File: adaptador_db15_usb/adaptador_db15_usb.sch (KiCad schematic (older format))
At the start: 3 parts, among them J1 Conn_01x34, J2 A-USB3_A-LP-SMT1, J3 A-USB3_A-LP-SMT1

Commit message: Fixed adapter pins connections
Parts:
- J2, J3: symbol A-USB3_A-LP-SMT1:A-USB3_A-LP-SMT1 -> adaptador_db15_usb-rescue:A-USB3_A-LP-SMT1-A-USB3_A-LP-SMT1
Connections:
- wire segments 70 -> 122
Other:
- moved on the sheet: J1
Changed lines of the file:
@@
 EESchema Schematic File Version 4
-LIBS:adaptador_db15_usb-cache
-EELAYER 26 0
+EELAYER 30 0
 EELAYER END
 $Descr A4 11693 8268
@@
 L Connector_Generic:Conn_01x34 J1
 U 1 1 60786015
-P 3550 4300
-F 0 "J1" H 3470 6117 50  0000 C CNN
-F 1 "Conn_01x34" H 3470 6026 50  0000 C CNN
-F 2 "kl25z:DSUB-15-HD_F_D" H 3550 4300 50  0001 C CNN
-F 3 "~" H 3550 4300 50  0001 C CNN
-	1    3550 4300
+P 2589 4300
+F 0 "J1" H 2509 6117 50  0000 C CNN
+F 1 "Conn_01x34" H 2509 6026 50  0000 C CNN
+F 2 "kl25z:DSUB-15-HD_F_D" H 2589 4300 50  0001 C CNN
+F 3 "~" H 2589 4300 50  0001 C CNN
+	1    2589 4300
 	-1   0    0    -1
 $EndComp
 $Comp
-L A-USB3_A-LP-SMT1:A-USB3_A-LP-SMT1 J2
+L adaptador_db15_usb-rescue:A-USB3_A-LP-SMT1-A-USB3_A-LP-SMT1 J2
 U 1 1 607860AA
 P 7000 3250
@@
 $EndComp
 $Comp
-L A-USB3_A-LP-SMT1:A-USB3_A-LP-SMT1 J3
+L adaptador_db15_usb-rescue:A-USB3_A-LP-SMT1-A-USB3_A-LP-SMT1 J3
 U 1 1 60786146
 P 7000 4750
@@
 $EndComp
 Wire Wire Line
-	3750 5700 4100 5700
-Wire Wire Line
 	4100 5700 4100 5800
-Wire Wire Line
-	4100 6000 3750 6000
-Wire Wire Line
-	3750 5800 4100 5800
 Connection ~ 4100 5800
 Wire Wire Line
 	4100 5800 4100 5900
-Wire Wire Line
-	3750 5900 4100 5900
 Connection ~ 4100 5900
 Wire Wire Line
@@
 EndData
 $EndBitmap
-Wire Wire Line
-	3750 3800 4500 3800
 Text Label 4050 3000 0    50   ~ 0
 up1
@@
 Text Label 4050 4100 0    50   ~ 0
 -clock1
-Wire Wire Line
-	3750 4200 4500 4200
-Wire Wire Line
-	3750 4400 4500 4400
-Wire Wire Line
-	4500 4700 3750 4700
-Wire Wire Line
-	3750 4800 4500 4800
-Wire Wire Line
-	4500 5000 3750 5000
-Wire Wire Line
-	4500 5200 3750 5200
-Wire Wire Line
-	3750 5300 4500 5300
-Wire Wire Line
-	3750 5500 4500 5500
 Text Label 3750 4200 0    50   ~ 0
 [1]
@@
 NoConn ~ 6600 2750
 Wire Wire Line
-	3750 3100 5500 3100
-Wire Wire Line
 	5500 3100 5500 3450
 Wire Wire Line
 	5500 3450 6600 3450
 Wire Wire Line
-	3750 3900 5550 3900
-Wire Wire Line
 	5550 3900 5550 3550
 Wire Wire Line
 	5550 3550 6600 3550
 Wire Wire Line
-	3750 3400 5550 3400
-Wire Wire Line
 	5550 3400 5550 3150
 Wire Wire Line
 	5550 3150 6600 3150
 Wire Wire Line
-	3750 4100 5600 4100
-Wire Wire Line
 	5600 4100 5600 3250
 Wire Wire Line
@@
 	5450 2850 6600 2850
 Wire Wire Line
-	3750 3600 5450 3600
-Wire Wire Line
 	5400 2800 5400 2950
 Wire Wire Line
 	5400 2950 6250 2950
-Wire Wire Line
-	3750 2800 5400 2800
 Wire Wire Line
 	6600 3050 6250 3050
@@
 Wire Wire Line
 	5350 3350 6600 3350
-Wire Wire Line
-	3750 3000 5350 3000
 NoConn ~ 4500 3800
 Wire Wire Line
@@
 	5350 4850 6600 4850
 Wire Wire Line
-	3750 4300 5400 4300
-Wire Wire Line
-	3750 4500 5350 4500
-Wire Wire Line
-	3750 4600 5500 4600
-Wire Wire Line
-	3750 4900 5550 4900
-Wire Wire Line
-	3750 5100 5450 5100
-Wire Wire Line
-	3750 5400 5550 5400
-Wire Wire Line
-	3750 5600 5600 5600
-Wire Wire Line
 	6600 5250 6600 5700
 Connection ~ 6600 5700
 Wire Wire Line
 	6600 5700 8650 5700
+Wire Wire Line
+	2789 5700 4100 5700
+Wire Wire Line
+	2789 6000 4100 6000
+Wire Wire Line
+	2789 5800 4100 5800
+Wire Wire Line
+	2789 5900 4100 5900
+Wire Wire Line
+	3140 2700 3140 4200
+Wire Wire Line
+	3159 2800 3159 4300
+Wire Wire Line
+	3179 2900 3179 4400
+Wire Wire Line
+	3199 3000 3199 4500
+Wire Wire Line
+	3219 3100 3219 4600
+Wire Wire Line
+	3239 3200 3239 4700
+Wire Wire Line
+	3258 3300 3258 4800
+Wire Wire Line
+	3278 3400 3278 4900
+Wire Wire Line
+	3298 3500 3298 5000
+Wire Wire Line
+	3318 3600 3318 5100
+Wire Wire Line
+	3339 3700 3339 5200
+Wire Wire Line
+	3358 3800 3358 5300
+Wire Wire Line
+	3378 3900 3378 5400
+Wire Wire Line
+	3398 4000 3398 5500
+Wire Wire Line
+	3418 4100 3418 5600
+Wire Wire Line
+	2789 2700 3140 2700
+Wire Wire Line
+	2789 2800 3159 2800
+Wire Wire Line
+	2789 2900 3179 2900
+Wire Wire Line
+	2789 3000 3199 3000
+Wire Wire Line
+	2789 3100 3219 3100
+Wire Wire Line
+	2789 3200 3239 3200
+Wire Wire Line
+	2789 3300 3258 3300
+Wire Wire Line
+	2789 3400 3278 3400
+Wire Wire Line
+	2789 3500 3298 3500
+Wire Wire Line
+	2789 3600 3318 3600
+Wire Wire Line
+	2789 3700 3339 3700
+Wire Wire Line
+	2789 3800 3358 3800
+Wire Wire Line
+	2789 3900 3378 3900
+Wire Wire Line
+	2789 4000 3398 4000
+Wire Wire Line
+	2789 4100 3418 4100
+Wire Wire Line
+	2789 4200 3140 4200
+Wire Wire Line
+	2789 4400 3179 4400
+Wire Wire Line
+	2789 4700 3239 4700
+Wire Wire Line
+	2789 4800 3258 4800
+Wire Wire Line
+	2789 5000 3298 5000
+Wire Wire Line
+	2789 5200 3339 5200
+Wire Wire Line
+	2789 5300 3358 5300
+Wire Wire Line
+	2789 5500 3398 5500
+Wire Wire Line
+	2789 4300 3159 4300
+Wire Wire Line
+	2789 4500 3199 4500
+Wire Wire Line
+	2789 4600 3219 4600
+Wire Wire Line
+	2789 4900 3278 4900
+Wire Wire Line
+	2789 5100 3318 5100
+Wire Wire Line
+	2789 5400 3378 5400
+Wire Wire Line
+	2789 5600 3418 5600
+Connection ~ 3140 2700
+Wire Wire Line
+	3140 2700 3750 2700
+Connection ~ 3140 4200
+Wire Wire Line
+	3140 4200 4500 4200
+Connection ~ 3159 2800
+Wire Wire Line
+	3159 2800 5400 2800
+Connection ~ 3159 4300
+Wire Wire Line
+	3159 4300 5400 4300
+Connection ~ 3179 2900
+Wire Wire Line
+	3179 2900 3750 2900
+Connection ~ 3179 4400
+Wire Wire Line
+	3179 4400 4500 4400
+Connection ~ 3199 3000
+Wire Wire Line
+	3199 3000 5350 3000
+Connection ~ 3199 4500
+Wire Wire Line
+	3199 4500 5350 4500
+Connection ~ 3219 3100
+Wire Wire Line
+	3219 3100 5500 3100
+Connection ~ 3219 4600
+Wire Wire Line
+	3219 4600 5500 4600
+Connection ~ 3239 3200
+Wire Wire Line
+	3239 3200 3750 3200
+Connection ~ 3239 4700
+Wire Wire Line
+	3239 4700 4500 4700
+Connection ~ 3258 3300
+Wire Wire Line
+	3258 3300 3750 3300
+Connection ~ 3258 4800
+Wire Wire Line
+	3258 4800 4500 4800
+Connection ~ 3278 3400
+Wire Wire Line
+	3278 3400 5550 3400
+Connection ~ 3278 4900
+Wire Wire Line
+	3278 4900 5550 4900
+Connection ~ 3298 3500
+Wire Wire Line
+	3298 3500 3750 3500
+Connection ~ 3298 5000
+Wire Wire Line
+	3298 5000 4500 5000
+Connection ~ 3318 3600
+Wire Wire Line
+	3318 3600 5450 3600
+Connection ~ 3318 5100
+Wire Wire Line
+	3318 5100 5450 5100
+Connection ~ 3339 3700
+Wire Wire Line
+	3339 3700 3750 3700
+Connection ~ 3339 5200
+Wire Wire Line
+	3339 5200 4500 5200
+Connection ~ 3358 3800
+Wire Wire Line
+	3358 3800 4500 3800
+Connection ~ 3358 5300
+Wire Wire Line
+	3358 5300 4500 5300
+Connection ~ 3378 3900
+Wire Wire Line
+	3378 3900 5550 3900
+Connection ~ 3378 5400
+Wire Wire Line
+	3378 5400 5550 5400
+Connection ~ 3398 4000
+Wire Wire Line
+	3398 4000 3750 4000
+Connection ~ 3398 5500
+Wire Wire Line
+	3398 5500 4500 5500
+Connection ~ 3418 4100
+Wire Wire Line
+	3418 4100 5600 4100
+Connection ~ 3418 5600
+Wire Wire Line
+	3418 5600 5600 5600
 $EndSCHEMATC

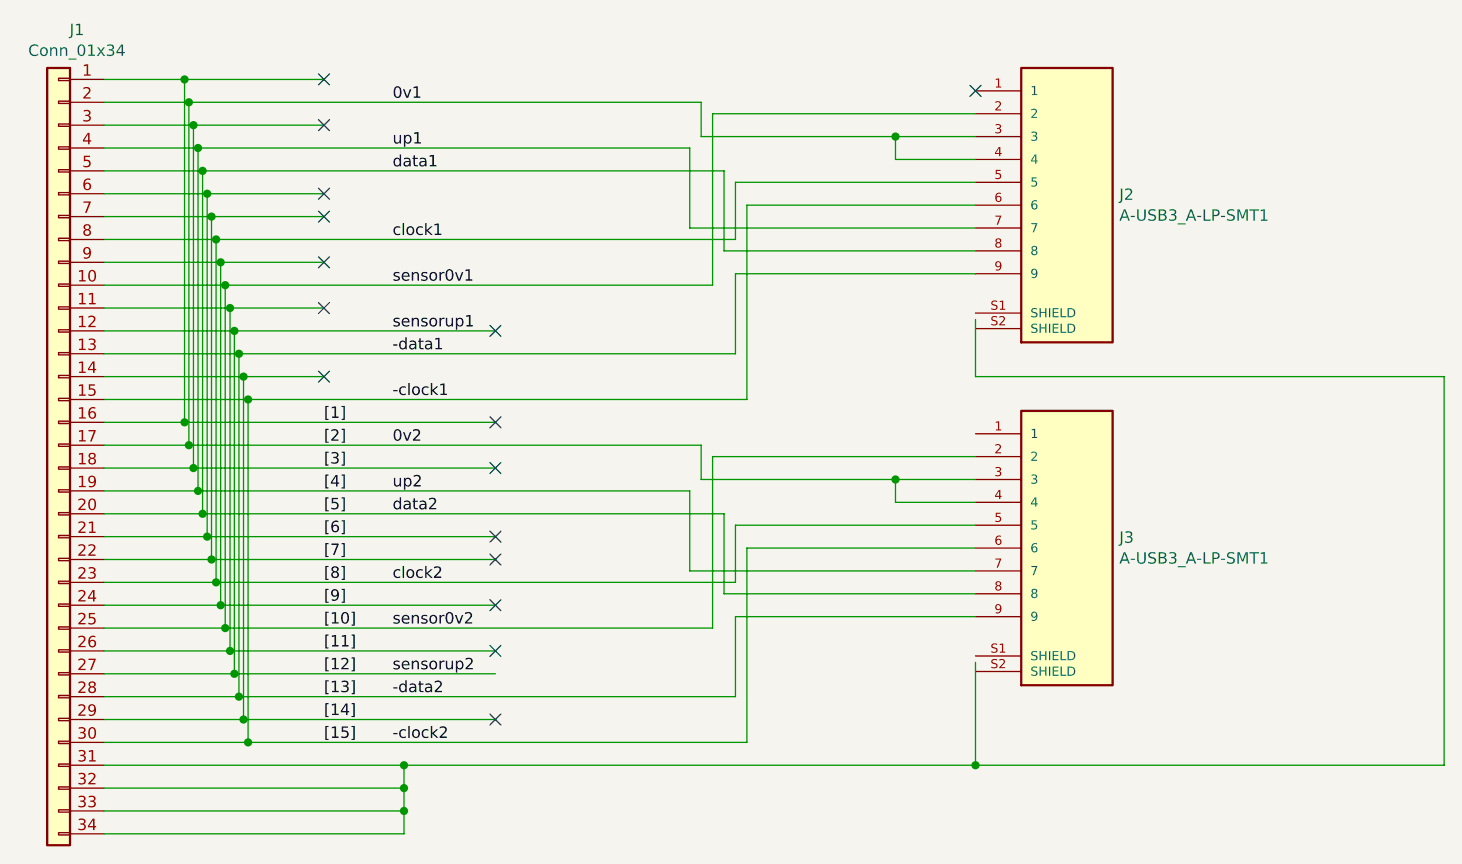
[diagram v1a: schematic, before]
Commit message: Fixed adapter pins connections
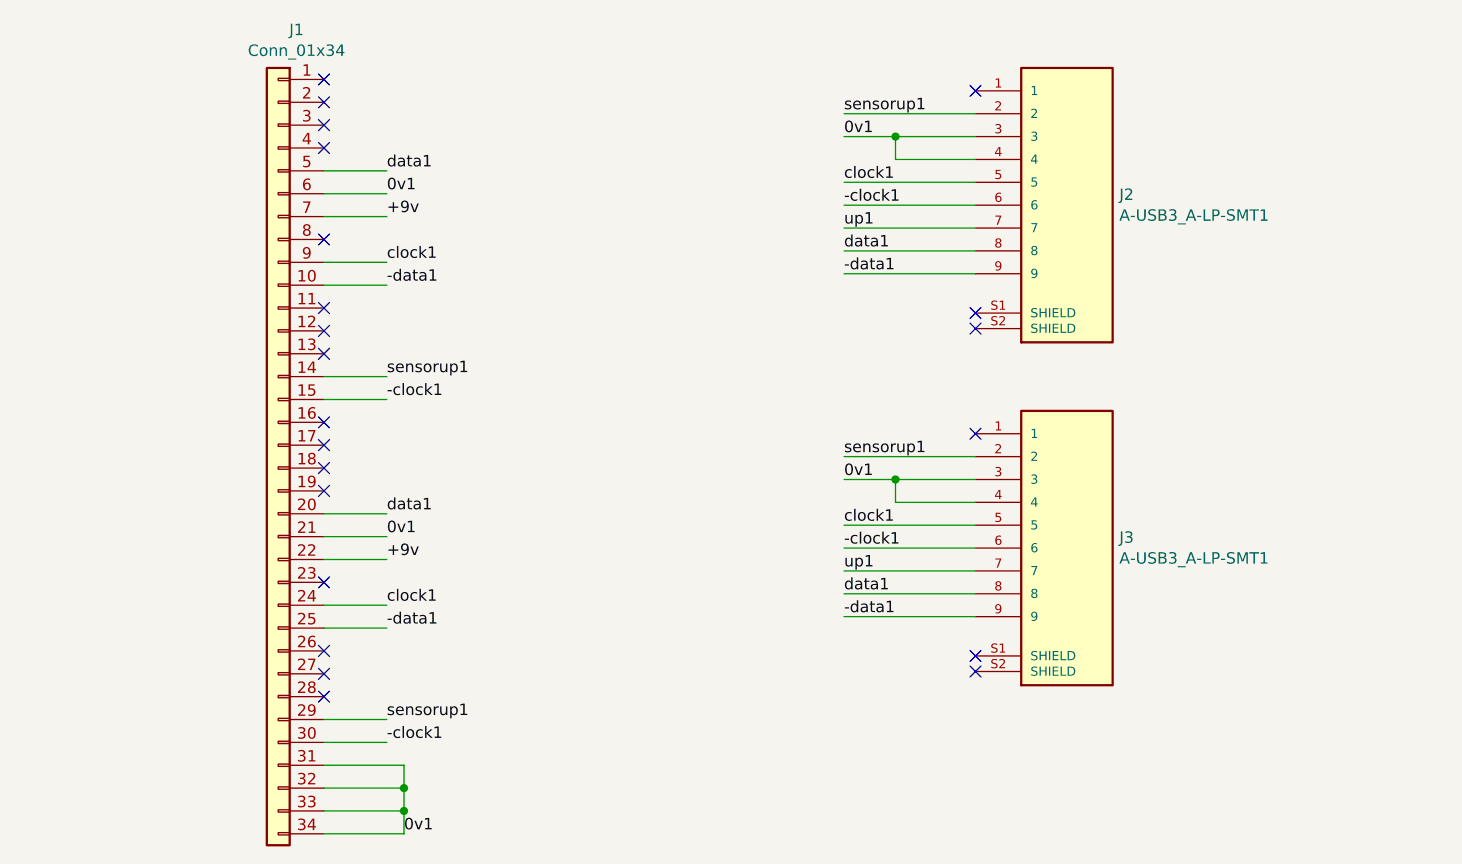
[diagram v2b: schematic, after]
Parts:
- J2: footprint A-USB3_A-LP-SMT1:ASSMANN_A-USB3_A-LP-SMT1 -> ASSMANN_A-USB3_A-LP-SMT1
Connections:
- net labels added: +9v
- net labels removed: -clock2, -data2, 0v2, [10], [11], [12], [13], [14], [15], [1], [2], [3], [4], [5], [6], [7], [8], [9], clock2, data2, sensor0v1, sensor0v2, sensorup2, up2
- wire segments 122 -> 41
- no-connect marks 16 -> 22
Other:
- moved on the sheet: J1
